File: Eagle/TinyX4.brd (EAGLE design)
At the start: 44.5 x 25.4 mm, 17 parts

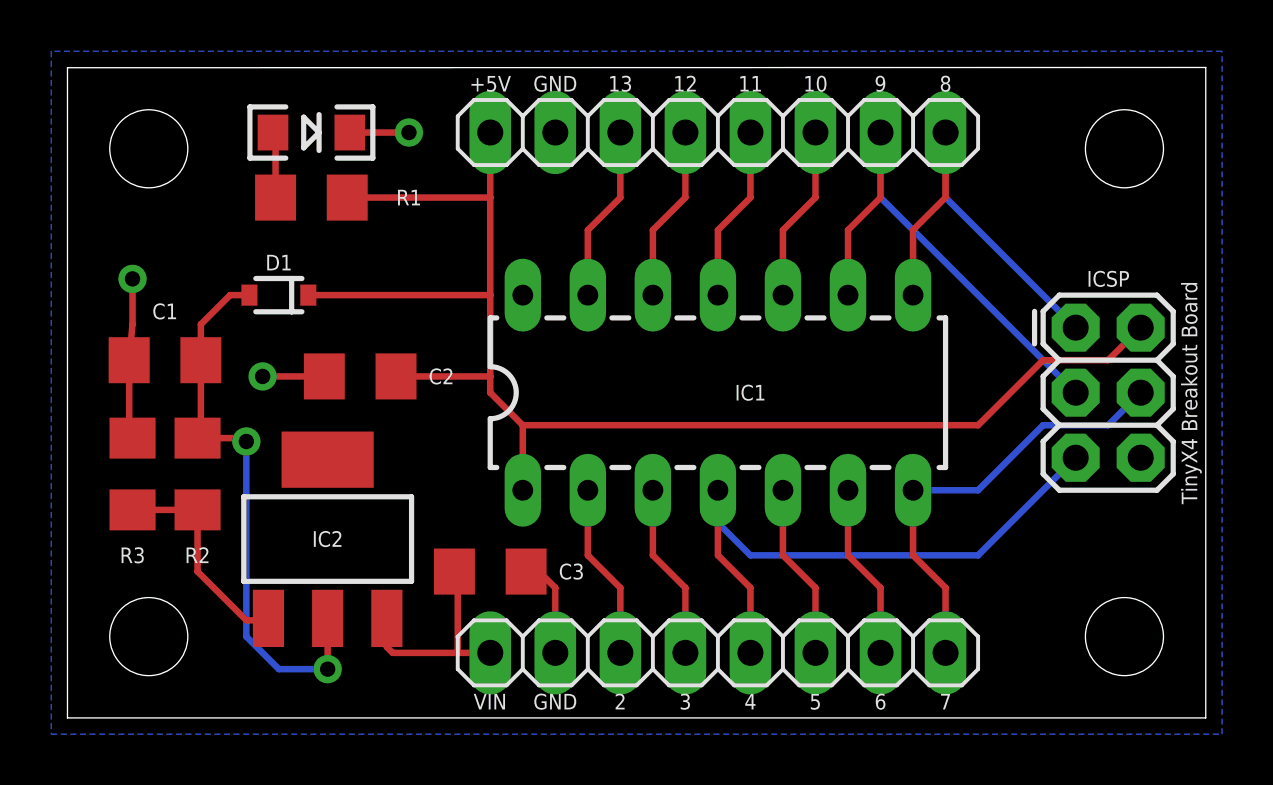
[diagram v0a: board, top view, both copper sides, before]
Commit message: added gebers, updated readme
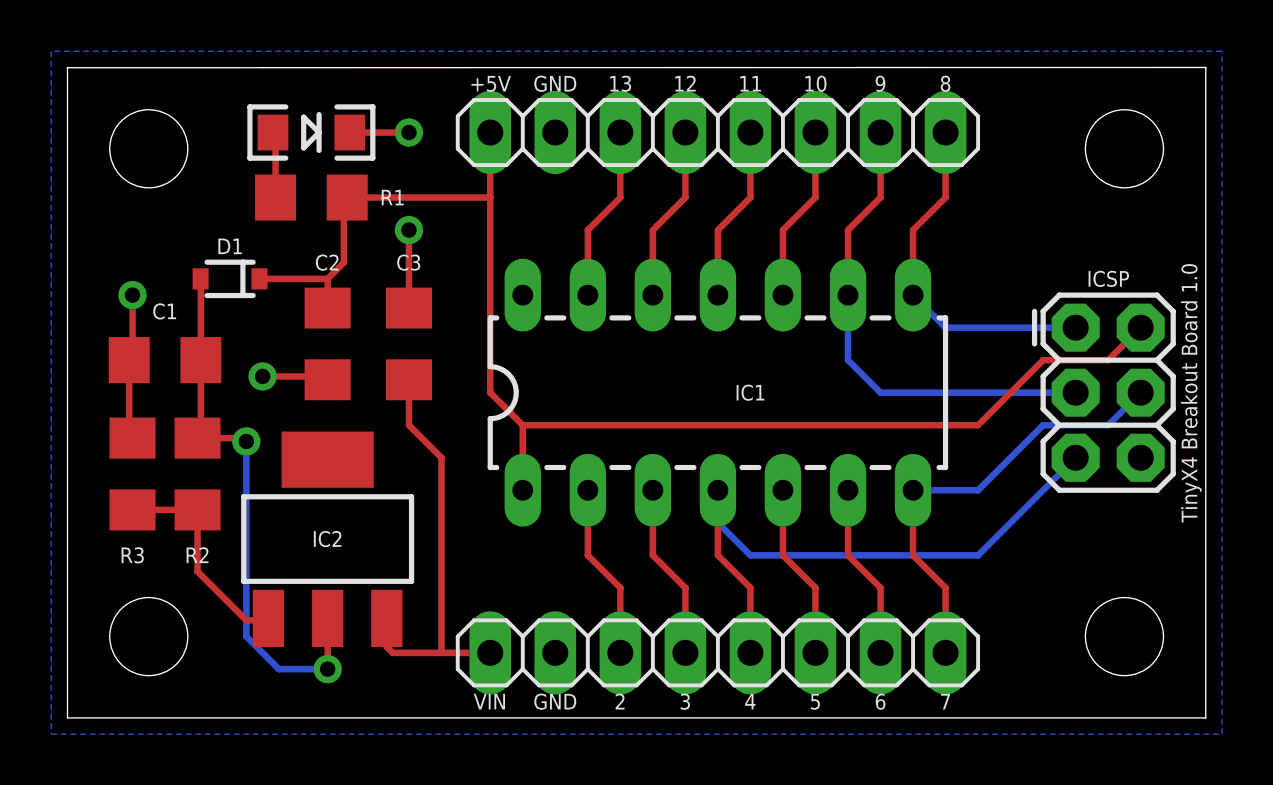
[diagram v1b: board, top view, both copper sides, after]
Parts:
- moved C3 9.44 mm to (13.3, 14.6), turned to 90 degrees
- moved D1 2.01 mm to (6.35, 17.1)
- moved C2 1.80 mm to (10.2, 14.6), turned to 270 degrees
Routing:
- net VIN: track 8.48 -> 16.4 mm
- net +5V: track 56.6 -> 53.1 mm
- net PIN8: track 16.6 -> 13.8 mm
- net PIN9: track 20.2 -> 18.8 mm
- net GND: track 14.9 -> 13.6 mm, vias 3 -> 4
- net N$2: track 22.3 -> 21.7 mm
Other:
- board text added: "TinyX4 Breakout Board 1.0"
- board text removed: "Rev 1.0"
- board text removed: "TinyX4 Breakout Board"
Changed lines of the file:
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@@
 <text x="24.13" y="24.765" size="0.6096" layer="121" align="center">12</text>
 <text x="21.59" y="24.765" size="0.6096" layer="121" align="center">13</text>
-<text x="43.815" y="12.7" size="0.6096" layer="121" rot="R90" align="center">TinyX4 Breakout Board</text>
+<text x="43.815" y="12.7" size="0.6096" layer="121" rot="R90" align="center">TinyX4 Breakout Board 1.0</text>
 <text x="0.635" y="12.7" size="0.6096" layer="122" rot="R270" align="center">(c) 2013 Andy Kipp</text>
-<text x="9.525" y="0.635" size="0.6096" layer="122" align="center">Rev 1.0</text>
 </plain>
 <attributes>
@@
 </element>
 <element name="R1" library="SparkFun-Resistors" package="1206" value="330" x="9.525" y="20.32" smashed="yes">
-<attribute name="NAME" x="13.335" y="20.32" size="0.6096" layer="25" align="center"/>
-</element>
-<element name="C2" library="SparkFun-Capacitors" package="1206" value="0.1uF" x="11.43" y="13.335" smashed="yes" rot="R180">
-<attribute name="NAME" x="14.605" y="13.335" size="0.6096" layer="25" rot="R180" align="center"/>
+<attribute name="NAME" x="12.7" y="20.32" size="0.6096" layer="25" align="center"/>
+</element>
+<element name="C2" library="SparkFun-Capacitors" package="1206" value="0.1uF" x="10.16" y="14.605" smashed="yes" rot="R270">
+<attribute name="NAME" x="10.16" y="17.78" size="0.6096" layer="25" align="center"/>
 </element>
 <element name="IC2" library="SparkFun-PowerIC" package="SOT223" value="" x="10.16" y="6.985" smashed="yes">
@@
 <attribute name="VALUE" x="9.0805" y="6.7945" size="0.4064" layer="27"/>
 </element>
-<element name="D1" library="SparkFun-DiscreteSemi" package="SOD-323" value="" x="8.255" y="16.51" smashed="yes" rot="R180">
-<attribute name="NAME" x="8.255" y="17.78" size="0.6096" layer="25" rot="R180" align="center"/>
-<attribute name="VALUE" x="9.271" y="17.907" size="0.4064" layer="27" rot="R180"/>
+<element name="D1" library="SparkFun-DiscreteSemi" package="SOD-323" value="" x="6.35" y="17.145" smashed="yes" rot="R180">
+<attribute name="NAME" x="6.35" y="18.415" size="0.6096" layer="25" rot="R180" align="center"/>
+<attribute name="VALUE" x="7.366" y="18.542" size="0.4064" layer="27" rot="R180"/>
 </element>
 <element name="R2" library="SparkFun-Passives" package="1206" value="240" x="5.08" y="9.525" smashed="yes" rot="R90">
@@
 <attribute name="NAME" x="3.81" y="15.875" size="0.6096" layer="25" rot="R180" align="center"/>
 </element>
-<element name="C3" library="SparkFun-Capacitors" package="1206" value="10uF" x="16.51" y="5.715" smashed="yes">
-<attribute name="NAME" x="19.685" y="5.715" size="0.6096" layer="25" align="center"/>
+<element name="C3" library="SparkFun-Capacitors" package="1206" value="10uF" x="13.335" y="14.605" smashed="yes" rot="R90">
+<attribute name="NAME" x="13.335" y="17.78" size="0.6096" layer="25" rot="R180" align="center"/>
 </element>
 </elements>
@@
 <contactref element="IC2" pad="3"/>
 <contactref element="C3" pad="1"/>
-<wire x1="16.51" y1="2.54" x2="15.24" y2="2.54" width="0.254" layer="1"/>
-<wire x1="15.24" y1="2.54" x2="12.7" y2="2.54" width="0.254" layer="1"/>
+<wire x1="16.51" y1="2.54" x2="14.605" y2="2.54" width="0.254" layer="1"/>
+<wire x1="14.605" y1="2.54" x2="12.7" y2="2.54" width="0.254" layer="1"/>
 <wire x1="12.7" y1="2.54" x2="12.4714" y2="2.7686" width="0.254" layer="1"/>
 <wire x1="12.4714" y1="2.7686" x2="12.4714" y2="3.8862" width="0.254" layer="1"/>
-<wire x1="15.11" y1="5.715" x2="15.24" y2="5.585" width="0.254" layer="1"/>
-<wire x1="15.24" y1="5.585" x2="15.24" y2="2.54" width="0.254" layer="1"/>
+<wire x1="13.335" y1="13.205" x2="13.335" y2="11.43" width="0.254" layer="1"/>
+<wire x1="13.335" y1="11.43" x2="14.605" y2="10.16" width="0.254" layer="1"/>
+<wire x1="14.605" y1="10.16" x2="14.605" y2="2.54" width="0.254" layer="1"/>
 </signal>
 <signal name="+5V">
@@
 <wire x1="17.78" y1="11.43" x2="17.78" y2="8.89" width="0.254" layer="1"/>
 <wire x1="10.925" y1="20.32" x2="16.51" y2="20.32" width="0.254" layer="1"/>
-<wire x1="16.51" y1="20.32" x2="16.51" y2="16.51" width="0.254" layer="1"/>
-<wire x1="16.51" y1="16.51" x2="16.51" y2="13.335" width="0.254" layer="1"/>
-<wire x1="16.51" y1="13.335" x2="16.51" y2="12.7" width="0.254" layer="1"/>
+<wire x1="16.51" y1="20.32" x2="16.51" y2="12.7" width="0.254" layer="1"/>
 <wire x1="16.51" y1="12.7" x2="17.78" y2="11.43" width="0.254" layer="1"/>
-<wire x1="9.405" y1="16.51" x2="16.51" y2="16.51" width="0.254" layer="1"/>
 <wire x1="16.51" y1="20.32" x2="16.51" y2="22.86" width="0.254" layer="1"/>
-<wire x1="12.83" y1="13.335" x2="16.51" y2="13.335" width="0.254" layer="1"/>
+<wire x1="7.5" y1="17.145" x2="10.16" y2="17.145" width="0.254" layer="1"/>
+<wire x1="10.16" y1="17.145" x2="10.16" y2="16.005" width="0.254" layer="1"/>
+<wire x1="10.925" y1="20.32" x2="10.795" y2="20.19" width="0.254" layer="1"/>
+<wire x1="10.795" y1="20.19" x2="10.795" y2="17.78" width="0.254" layer="1"/>
+<wire x1="10.795" y1="17.78" x2="10.16" y2="17.145" width="0.254" layer="1"/>
 </signal>
 <signal name="N$1">
@@
 <contactref element="C3" pad="2"/>
 <contactref element="C1" pad="2"/>
-<wire x1="19.05" y1="2.54" x2="19.05" y2="5.08" width="0.254" layer="1"/>
-<wire x1="19.05" y1="5.08" x2="18.415" y2="5.715" width="0.254" layer="1"/>
-<wire x1="18.415" y1="5.715" x2="17.91" y2="5.715" width="0.254" layer="1"/>
 <wire x1="2.54" y1="10.925" x2="2.41" y2="11.055" width="0.254" layer="1"/>
 <wire x1="2.41" y1="11.055" x2="2.41" y2="13.97" width="0.254" layer="1"/>
-<wire x1="2.41" y1="13.97" x2="2.54" y2="15.37" width="0.254" layer="1"/>
-<wire x1="2.54" y1="15.37" x2="2.54" y2="17.145" width="0.254" layer="1"/>
-<via x="2.54" y="17.145" extent="1-16" drill="0.6"/>
+<wire x1="2.54" y1="14.1" x2="2.54" y2="16.51" width="0.254" layer="1"/>
+<via x="2.54" y="16.51" extent="1-16" drill="0.6"/>
+<wire x1="2.41" y1="13.97" x2="2.54" y2="14.1" width="0.254" layer="1"/>
+<wire x1="10.16" y1="13.205" x2="10.03" y2="13.335" width="0.254" layer="1"/>
 <wire x1="10.03" y1="13.335" x2="7.62" y2="13.335" width="0.254" layer="1"/>
 <via x="7.62" y="13.335" extent="1-16" drill="0.6"/>
+<wire x1="13.335" y1="16.005" x2="13.335" y2="19.05" width="0.254" layer="1"/>
+<via x="13.335" y="19.05" extent="1-16" drill="0.6"/>
 </signal>
 <signal name="PIN2">
@@
 <wire x1="34.29" y1="20.32" x2="34.29" y2="22.86" width="0.254" layer="1"/>
 <contactref element="ICSP" pad="1"/>
-<wire x1="39.37" y1="15.24" x2="34.29" y2="20.32" width="0.254" layer="16"/>
-<wire x1="34.29" y1="20.32" x2="34.29" y2="22.86" width="0.254" layer="16"/>
+<wire x1="39.37" y1="15.24" x2="34.29" y2="15.24" width="0.254" layer="16"/>
+<wire x1="34.29" y1="15.24" x2="33.02" y2="16.51" width="0.254" layer="16"/>
 </signal>
 <signal name="PIN10">
@@
 <wire x1="31.75" y1="22.86" x2="31.75" y2="20.32" width="0.254" layer="1"/>
 <wire x1="31.75" y1="20.32" x2="30.48" y2="19.05" width="0.254" layer="1"/>
+<contactref element="ICSP" pad="3"/>
 <wire x1="30.48" y1="19.05" x2="30.48" y2="16.51" width="0.254" layer="1"/>
-<contactref element="ICSP" pad="3"/>
-<wire x1="39.37" y1="12.7" x2="31.75" y2="20.32" width="0.254" layer="16"/>
-<wire x1="31.75" y1="20.32" x2="31.75" y2="22.86" width="0.254" layer="16"/>
+<wire x1="39.37" y1="12.7" x2="31.75" y2="12.7" width="0.254" layer="16"/>
+<wire x1="31.75" y1="12.7" x2="30.48" y2="13.97" width="0.254" layer="16"/>
+<wire x1="30.48" y1="13.97" x2="30.48" y2="16.51" width="0.254" layer="16"/>
 </signal>
 <signal name="PIN7">
@@
 <wire x1="5.21" y1="11.055" x2="5.21" y2="13.97" width="0.254" layer="1"/>
 <wire x1="5.21" y1="13.97" x2="5.08" y2="14.1" width="0.254" layer="1"/>
-<wire x1="7.105" y1="16.51" x2="6.35" y2="16.51" width="0.254" layer="1"/>
-<wire x1="6.35" y1="16.51" x2="5.21" y2="15.37" width="0.254" layer="1"/>
-<wire x1="5.21" y1="15.37" x2="5.21" y2="13.97" width="0.254" layer="1"/>
+<wire x1="5.2" y1="17.145" x2="5.21" y2="17.135" width="0.254" layer="1"/>
+<wire x1="5.21" y1="17.135" x2="5.21" y2="13.97" width="0.254" layer="1"/>
 </signal>
 <signal name="N$3">
